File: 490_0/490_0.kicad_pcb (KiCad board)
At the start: 4 copper layers, 208.5 x 137.8 mm, 192 parts, among them J1 PAD, J10 PAD, J11 S3B-XH-A, J12 2000-1-1-20-00-BK, J13 S2B-ZR, J15 S3B-XH-A, J16 DF40HC(3.0)-100DS-0.4V(58), J17 DF40HC(3.0)-100DS-0.4V(58), J18 TS-103-G-A, J19 467650301, J2 PAD, J20 YO0201500000G, J21 TS-102-G-A, J22 2000-1-1-20-00-BK, J23 S3B-XH-A, J3 PAD, J4 PAD, J5 PAD, J6 PAD, J7 629105150521, J8 0526101571, J9 PAD, Q1 AO3400A, Q2 AO3400A, Q3 AO3400A, Q4 AO3400A, Q5 AO3400A, Q6 BSS84, SW1 TL2230EEF140, SW2 TL1105LF160Q, SW3 TL1105LF160Q, SW4 TL1105LF160Q, SW5 TL1105LF160Q, SW6 TL1105LF160Q, SW7 TL1105LF160Q, SW8 TL1105LF160Q, U1 MAX98357A, U10 EMI8142MUTAG, U11 SP3003-02XTG, U12 TPD8S009DSMR, U13 SP3003-02XTG, U14 SP3003-02XTG, U15 SP3003-02XTG, U16 SP3003-02XTG, U17 SP3003-02XTG, U18 TPD8S009DSMR, U19 SP3003-02XTG, U2 TPS2553DBVR, U3 TPS2553DBVR, U4 USB2512B-I/M2, U5 TS3USB221AQRSERQ1, U6 PCA9685, U7 TPS566247DRLR, U8 MP2639AGR-Z, U9 EMI8142MUTAG, Y1 24M20P2/XT324-10/10

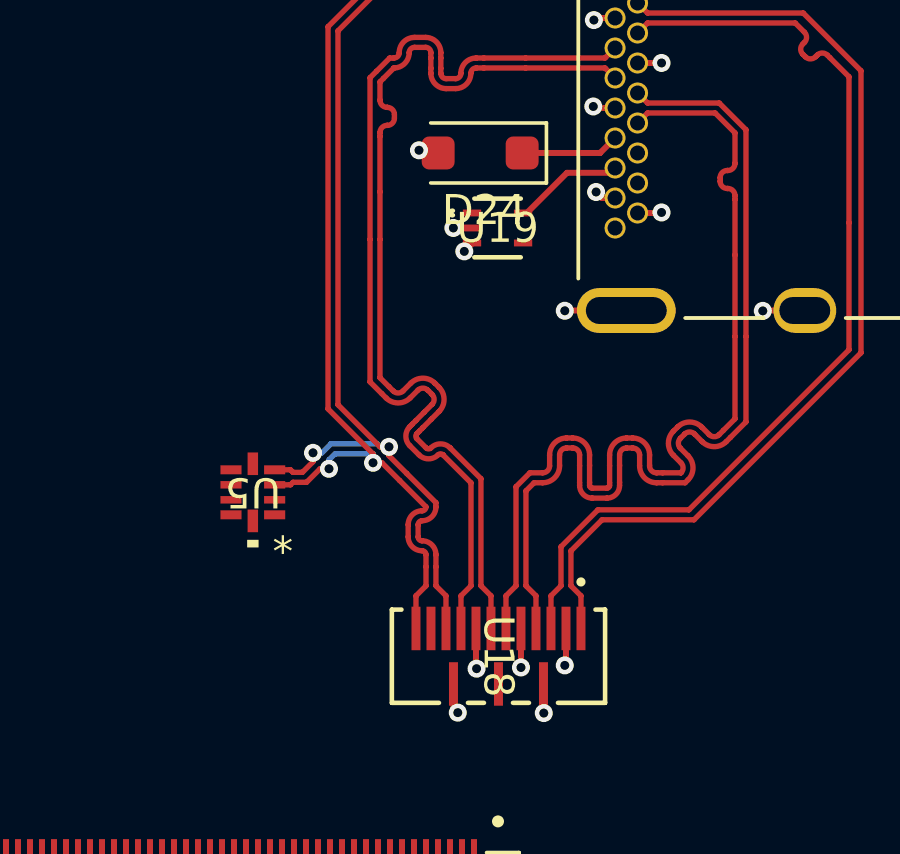
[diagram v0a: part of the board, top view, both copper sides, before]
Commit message: Finished ESD diff pairs routing
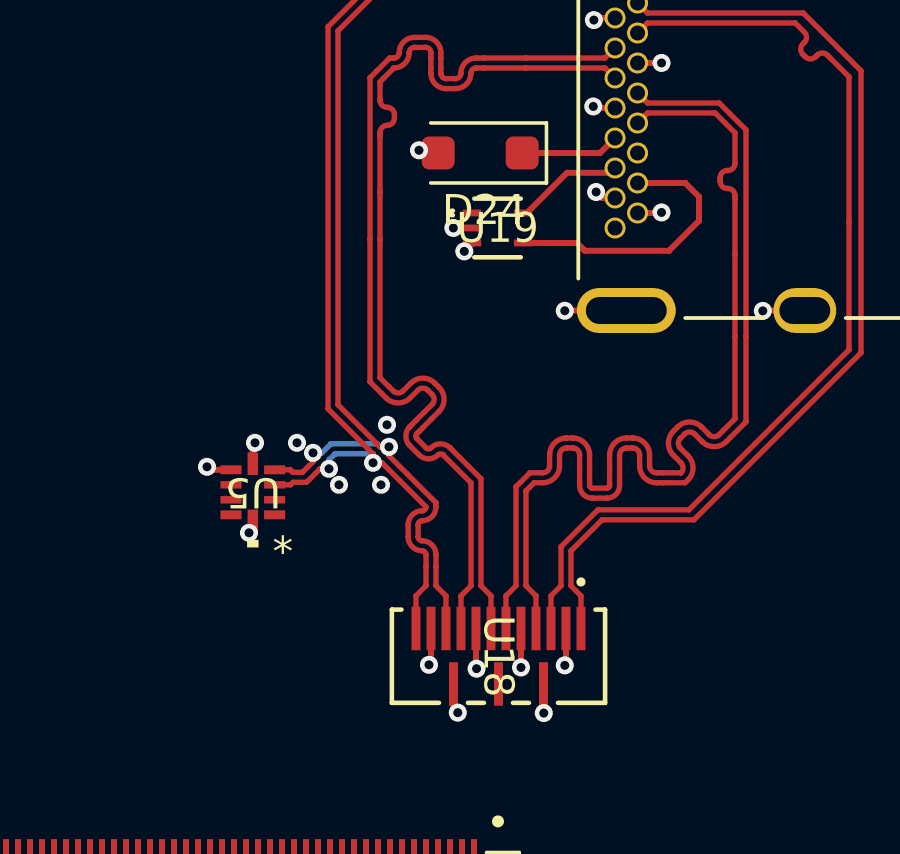
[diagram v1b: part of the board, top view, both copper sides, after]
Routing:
- net /PCB1/PCB1-Board Connector A/SDA1: track 0.00 -> 9.43 mm
- net GND: track 22.3 -> 25.1 mm, vias 17 -> 24
- net +3.3V: track 3.26 -> 3.71 mm, vias 4 -> 5
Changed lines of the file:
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@@
 	)
 	(segment
+		(start 127.865988 127.934012)
+		(end 127.8 128)
+		(width 0.2)
+		(layer "F.Cu")
+		(net 2)
+	)
+	(segment
 		(start 138.786889 101.689655)
 		(end 138.775989 101.678755)
@@
 	)
 	(segment
+		(start 121.9274 121.297556)
+		(end 121.9274 120.6726)
+		(width 0.2)
+		(layer "F.Cu")
+		(net 2)
+	)
+	(segment
 		(start 138.939513 116.189655)
 		(end 138.92689 116.202278)
@@
 	)
 	(segment
+		(start 121.9274 120.6726)
+		(end 122 120.6)
+		(width 0.2)
+		(layer "F.Cu")
+		(net 2)
+	)
+	(segment
 		(start 133.326889 109.439655)
 		(end 133.275989 109.388755)
@@
 	)
 	(segment
+		(start 127.865988 126.788755)
+		(end 127.865988 127.934012)
+		(width 0.2)
+		(layer "F.Cu")
+		(net 2)
+	)
+	(segment
 		(start 133.365089 106.439655)
 		(end 133.295989 106.508755)
@@
 	)
 	(segment
+		(start 120.499999 121.499999)
+		(end 120.4 121.4)
+		(width 0.2)
+		(layer "F.Cu")
+		(net 2)
+	)
+	(segment
+		(start 121.2 121.499999)
+		(end 120.499999 121.499999)
+		(width 0.2)
+		(layer "F.Cu")
+		(net 2)
+	)
+	(segment
 		(start 124.82 87.96)
 		(end 124.82 87.21)
@@
 	)
 	(via
+		(at 126.2 122)
+		(size 0.6)
+		(drill 0.3)
+		(layers "F.Cu" "B.Cu")
+		(net 2)
+	)
+	(via
 		(at 133.295989 106.508755)
 		(size 0.6)
@@
 	)
 	(via
+		(at 127.8 128)
+		(size 0.6)
+		(drill 0.3)
+		(layers "F.Cu" "B.Cu")
+		(net 2)
+	)
+	(via
 		(at 128.611366 113.438757)
 		(size 0.6)
@@
 	)
 	(via
+		(at 124.8 122)
+		(size 0.6)
+		(drill 0.3)
+		(layers "F.Cu" "B.Cu")
+		(net 2)
+	)
+	(via
+		(at 120.4 121.4)
+		(size 0.6)
+		(drill 0.3)
+		(layers "F.Cu" "B.Cu")
+		(net 2)
+	)
+	(via
 		(at 122.07 89.71)
 		(size 0.6)
@@
 		(net 2)
 	)
+	(via
+		(at 122 120.6)
+		(size 0.6)
+		(drill 0.3)
+		(layers "F.Cu" "B.Cu")
+		(net 2)
+	)
+	(via
+		(at 123.4 120.6)
+		(size 0.6)
+		(drill 0.3)
+		(layers "F.Cu" "B.Cu")
+		(net 2)
+	)
+	(via
+		(at 126.4 120)
+		(size 0.6)
+		(drill 0.3)
+		(layers "F.Cu" "B.Cu")
+		(net 2)
+	)
 	(segment
 		(start 131.615989 128.638637)
@@
 	)
 	(segment
+		(start 121.9274 123.4726)
+		(end 121.8 123.6)
+		(width 0.2)
+		(layer "F.Cu")
+		(net 3)
+	)
+	(segment
 		(start 128.615989 129.578755)
 		(end 128.631678 129.594444)
@@
 		(net 3)
 	)
+	(segment
+		(start 121.9274 123.202444)
+		(end 121.9274 123.4726)
+		(width 0.2)
+		(layer "F.Cu")
+		(net 3)
+	)
+	(via
+		(at 121.8 123.6)
+		(size 0.6)
+		(drill 0.3)
+		(layers "F.Cu" "B.Cu")
+		(net 3)
+	)
 	(via
 		(at 128.75989 129.594444)
@@
 	)
 	(segment
+		(start 136.8 113.2)
+		(end 136.8 112.4)
+		(width 0.2)
+		(layer "F.Cu")
+		(net 114)
+	)
+	(segment
+		(start 135.8 114.2)
+		(end 136.8 113.2)
+		(width 0.2)
+		(layer "F.Cu")
+		(net 114)
+	)
+	(segment
+		(start 132.738755 113.938755)
+		(end 133 114.2)
+		(width 0.2)
+		(layer "F.Cu")
+		(net 114)
+	)
+	(segment
+		(start 130.935989 113.938755)
+		(end 132.738755 113.938755)
+		(width 0.2)
+		(layer "F.Cu")
+		(net 114)
+	)
+	(segment
+		(start 133 114.2)
+		(end 135.8 114.2)
+		(width 0.2)
+		(layer "F.Cu")
+		(net 114)
+	)
+	(segment
+		(start 136.8 112.4)
+		(end 136.339655 111.939655)
+		(width 0.2)
+		(layer "F.Cu")
+		(net 114)
+	)
+	(segment
+		(start 136.339655 111.939655)
+		(end 134.751811 111.939655)
+		(width 0.2)
+		(layer "F.Cu")
+		(net 114)
+	)
+	(segment

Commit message: Changed microHDMI to normal HDMI because of the footprint
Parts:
- moved C50 215.2 mm to (173.4, 129.6), turned to 90 degrees
- moved J19 213.2 mm to (176.4, 138.4)
- moved U13 211.2 mm to (171.3, 127.1)
- moved U14 210.0 mm to (167.3, 128.1)
- moved U10 209.5 mm to (170.4, 136.0), turned to 180 degrees
- moved U9 209.3 mm to (177.0, 127.2)
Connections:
- J19 pad 11: Net-(J19-TMDS_DATA_0-) -> /PCB1/PCB1-HDMI/D0-
- J19 pad 12: Net-(J19-TMDS_CLOCK+) -> /PCB1/PCB1-HDMI/CLK+
- J19 pad 14: Net-(J19-TMDS_CLOCK-) -> /PCB1/PCB1-HDMI/CLK-
- J19 pad 3: Net-(J19-TMDS_DATA_2+) -> /PCB1/PCB1-HDMI/D2-
- J19 pad 5: Net-(J19-TMDS_DATA_2-) -> /PCB1/PCB1-HDMI/D2+
- J19 pad 6: Net-(J19-TMDS_DATA_1+) -> /PCB1/PCB1-HDMI/D1-
- J19 pad 8: Net-(J19-TMDS_DATA_1-) -> /PCB1/PCB1-HDMI/D1+
- J19 pad 9: Net-(J19-TMDS_DATA_0+) -> /PCB1/PCB1-HDMI/D0+
- U10 pad 1: Net-(J19-TMDS_DATA_0+) -> unconnected-(U10-IN_1+-Pad1)
- U10 pad 10: /PCB1/PCB1-Board Connector A/HDMI0_TX0_P -> /PCB1/PCB1-Board Connector A/HDMI0_TX1_P
- U10 pad 2: Net-(J19-TMDS_DATA_0-) -> unconnected-(U10-IN_1−-Pad2)
- U10 pad 4: Net-(J19-TMDS_CLOCK+) -> unconnected-(U10-IN_2+-Pad4)
- U10 pad 5: Net-(J19-TMDS_CLOCK-) -> unconnected-(U10-IN_2--Pad5)
- U10 pad 9: /PCB1/PCB1-Board Connector A/HDMI0_TX0_N -> /PCB1/PCB1-Board Connector A/HDMI0_TX1_N
- U9 pad 1: Net-(J19-TMDS_DATA_1+) -> /PCB1/PCB1-HDMI/D0-
- U9 pad 10: /PCB1/PCB1-Board Connector A/HDMI0_TX1_N -> /PCB1/PCB1-Board Connector A/HDMI0_TX0_N
- U9 pad 2: Net-(J19-TMDS_DATA_1-) -> /PCB1/PCB1-HDMI/D0+
- U9 pad 4: Net-(J19-TMDS_DATA_2+) -> /PCB1/PCB1-HDMI/D2+
- U9 pad 5: Net-(J19-TMDS_DATA_2-) -> /PCB1/PCB1-HDMI/D2-
- U9 pad 6: /PCB1/PCB1-Board Connector A/HDMI0_TX2_P -> /PCB1/PCB1-Board Connector A/HDMI0_TX2_N
- U9 pad 7: /PCB1/PCB1-Board Connector A/HDMI0_TX2_N -> /PCB1/PCB1-Board Connector A/HDMI0_TX2_P
- U9 pad 9: /PCB1/PCB1-Board Connector A/HDMI0_TX1_P -> /PCB1/PCB1-Board Connector A/HDMI0_TX0_P
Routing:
- net /PCB1/PCB1-Board Connector A/USB_N: track 0.00 -> 21.1 mm
- net /PCB1/PCB1-Board Connector A/USB_P: track 0.00 -> 20.2 mm
- net +5V: track 7.64 -> 9.71 mm
- net GND: track 25.1 -> 26.1 mm, vias 24 -> 25

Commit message: Routing ESD to 100 pin connector
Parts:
- removed J19: 467650301, *CapStone*:MOLEX_467650301
- added J14: 2000-1-1-20-00-BK, *CapStone*:CNCTECH_2000-1-1-20-00-BK, F.Cu at (114.9, 159.5)
- moved D11 187.2 mm to (-90.8, 152.5)
- moved D12 187.2 mm to (-90.8, 148.5)
- moved D13 187.2 mm to (-91.0, 144.5)
- moved D14 187.2 mm to (-90.8, 140.5)
- moved R28 187.2 mm to (-85.8, 152.5)
- moved R30 187.2 mm to (-85.8, 148.5)
- moved R31 187.2 mm to (-86.0, 144.5)
- moved R33 187.2 mm to (-86.3, 140.5)
- moved U10 68.5 mm to (105.2, 157.2)
- moved C50 68.1 mm to (108.2, 149.3)
- moved U13 62.1 mm to (112.6, 147.2)
- moved U14 60.3 mm to (110.1, 147.1)
- moved U9 59.8 mm to (119.2, 142.5), turned to 180 degrees
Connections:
- U10 pad 1: unconnected-(U10-IN_1+-Pad1) -> /PCB1/PCB1-HDMI/D1-
- U10 pad 10: /PCB1/PCB1-Board Connector A/HDMI0_TX1_P -> /PCB1/PCB1-Board Connector A/HDMI0_TX1_N
- U10 pad 2: unconnected-(U10-IN_1−-Pad2) -> /PCB1/PCB1-HDMI/D1+
- U10 pad 4: unconnected-(U10-IN_2+-Pad4) -> /PCB1/PCB1-HDMI/CLK+
- U10 pad 5: unconnected-(U10-IN_2--Pad5) -> /PCB1/PCB1-HDMI/CLK-
- U10 pad 9: /PCB1/PCB1-Board Connector A/HDMI0_TX1_N -> /PCB1/PCB1-Board Connector A/HDMI0_TX1_P
- U13 pad 4: /PCB1/PCB1-Board Connector A/HDMI0_SCL -> /PCB1/PCB1-Board Connector A/HDMI0_CEC
- U14 pad 5: /PCB1/PCB1-Board Connector A/HDMI0_CEC -> /PCB1/PCB1-Board Connector A/HDMI0_SCL
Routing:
- net /PCB1/PCB1-Board Connector A/HDMI0_TX1_P: track 0.00 -> 42.1 mm, vias 0 -> 2
- net /PCB1/PCB1-Board Connector A/HDMI0_TX1_N: track 0.00 -> 40.5 mm, vias 0 -> 2
- net /PCB1/PCB1-Board Connector A/HDMI0_CLK_P: track 0.00 -> 35.7 mm, vias 0 -> 2
- net /PCB1/PCB1-Board Connector A/HDMI0_CLK_N: track 0.00 -> 34.1 mm, vias 0 -> 2
- net /PCB1/PCB1-Board Connector A/HDMI0_SDA: track 0.00 -> 25.1 mm
- net /PCB1/PCB1-HDMI/D1-: track 0.00 -> 15.3 mm
- net /PCB1/PCB1-HDMI/D2-: track 0.00 -> 15.3 mm
- net /PCB1/PCB1-HDMI/D1+: track 0.00 -> 15.3 mm
- net /PCB1/PCB1-HDMI/D2+: track 0.00 -> 15.2 mm
- net /PCB1/PCB1-HDMI/D0+: track 0.00 -> 15.2 mm
- net /PCB1/PCB1-HDMI/D0-: track 0.00 -> 15.2 mm
- net /PCB1/PCB1-HDMI/CLK+: track 0.00 -> 11.2 mm
- net /PCB1/PCB1-HDMI/CLK-: track 0.00 -> 10.7 mm
- net /PCB1/PCB1-Board Connector A/HDMI0_TX2_N: track 0.00 -> 10.6 mm, vias 0 -> 2
- net /PCB1/PCB1-Board Connector A/HDMI0_TX0_N: track 0.00 -> 10.3 mm
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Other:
- board size 208.5 x 137.8 mm -> 208.5 x 141.2 mm

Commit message: Final push
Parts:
- moved U9 6.88 mm to (124.0, 147.4)
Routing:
- net /PCB1/PCB1-Board Connector A/HDMI0_TX0_N: track 10.3 -> 0.00 mm
- net /PCB1/PCB1-Board Connector A/HDMI0_TX0_P: track 9.77 -> 0.00 mm
- net /PCB1/PCB1-Board Connector A/HDMI0_TX1_P: track 42.1 -> 35.1 mm
- net /PCB1/PCB1-Board Connector A/HDMI0_TX1_N: track 40.5 -> 35.7 mm
- net /PCB1/PCB1-Board Connector A/HDMI0_TX2_P: track 10.1 -> 13.8 mm
- net /PCB1/PCB1-Board Connector A/HDMI0_TX2_N: track 10.6 -> 13.2 mm
- net /PCB1/PCB1-HDMI/D2+: track 15.2 -> 14.6 mm
- net /PCB1/PCB1-HDMI/D0-: track 15.2 -> 14.6 mm

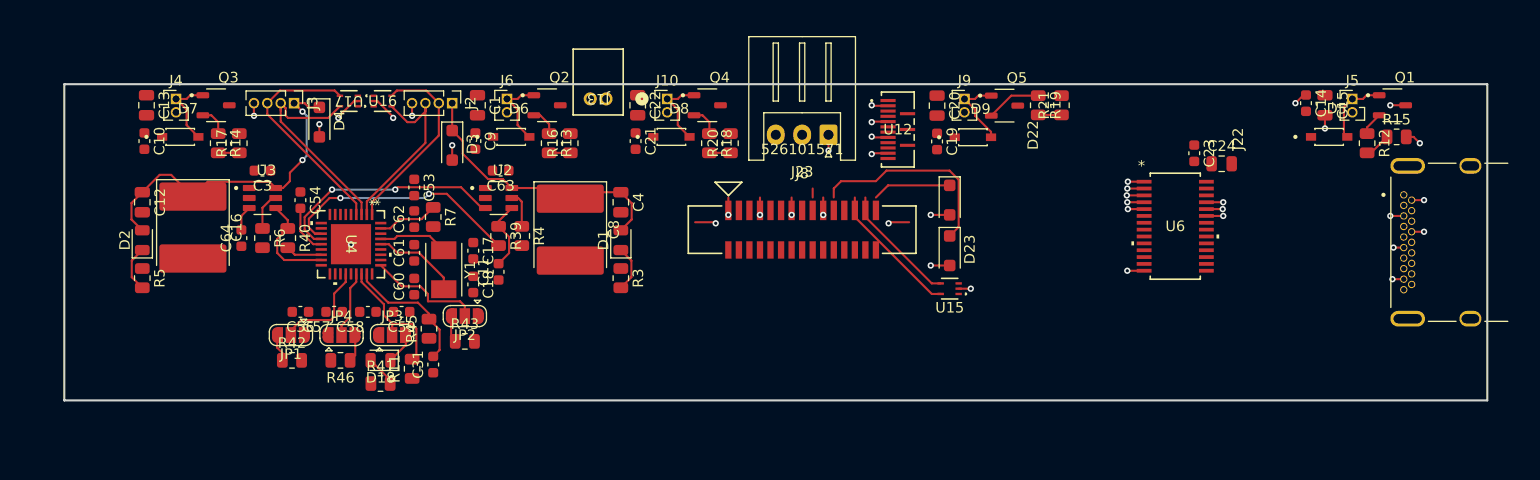
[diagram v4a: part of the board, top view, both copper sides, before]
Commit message: PCB merged, now schematic
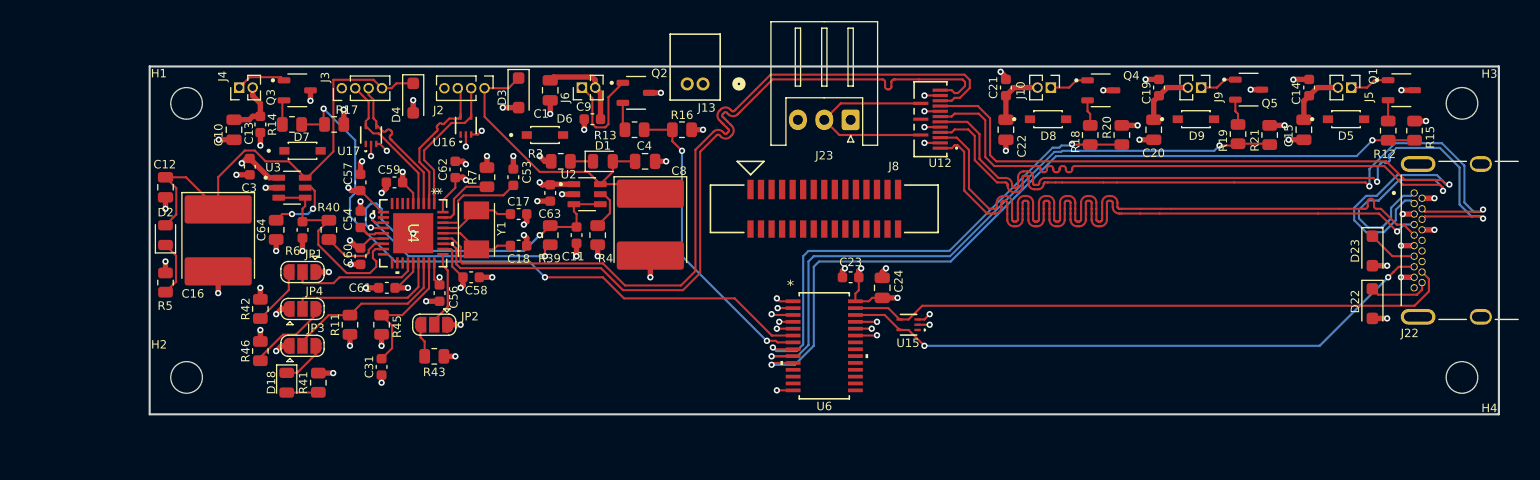
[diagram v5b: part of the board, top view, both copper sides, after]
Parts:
- added H1: MountingHole, MountingHole:MountingHole_3mm, F.Cu at (131.6, 22.0)
- added H2: MountingHole, MountingHole:MountingHole_3mm, F.Cu at (131.6, 48.0)
- added H3: MountingHole, MountingHole:MountingHole_3mm, F.Cu at (252.6, 22.0)
- added H4: MountingHole, MountingHole:MountingHole_3mm, F.Cu at (252.6, 48.0)
- moved D22 41.3 mm to (244.1, 41.0)
- moved D23 40.1 mm to (244.1, 36.0)
- moved Q4 37.4 mm to (218.3, 20.8)
- moved R20 37.1 mm to (220.3, 25.0)
- moved J10 36.4 mm to (213.6, 20.5), turned to -90 degrees
- moved R18 36.1 mm to (217.3, 25.0)
- moved D8 35.8 mm to (213.3, 23.5)
- moved C21 35.5 mm to (209.3, 20.5)
- moved U6 35.2 mm to (192.1, 45.0)
- moved C22 35.0 mm to (209.3, 24.5)
- moved C23 34.7 mm to (194.6, 38.5), turned to 0 degrees
- moved C24 34.3 mm to (197.6, 39.5), turned to 90 degrees
- moved Q5 23.2 mm to (232.4, 20.7)
- moved J9 22.5 mm to (227.9, 20.5), turned to -90 degrees
- moved C19 21.7 mm to (223.9, 20.5)
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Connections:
- net Net-(J22-D0+) renamed /PCB2/D0+
- net Net-(J22-D0-) renamed /PCB2/D0-
- net Net-(J22-D1+) renamed /PCB2/D1+
- net Net-(J22-D1-) renamed /PCB2/D1-
- J22 pad 1: /PCB2/PCB2-USB 2.0 Bridge/USB_P -> /PCB2/CK+
- J22 pad 10: Net-(J22-CK+) -> /PCB2/CK+
- J22 pad 12: Net-(J22-CK-) -> /PCB2/CK-
- J22 pad 3: /PCB2/PCB2-USB 2.0 Bridge/USB_N -> /PCB2/CK-
- J3 pad 1: VBUS2 -> GND_GLASSES
- J3 pad 2: /PCB2/PCB2-USB 2.0 Bridge/D2- -> /PCB2/PCB2-USB 2.0 Bridge/D2+
- J3 pad 3: /PCB2/PCB2-USB 2.0 Bridge/D2+ -> /PCB2/PCB2-USB 2.0 Bridge/D2-
- J3 pad 4: GND_GLASSES -> VBUS2
- U12 pad 10: /PCB2/PCB2-USB 2.0 Bridge/USB_P -> /PCB2/CK+
- U12 pad 12: /PCB2/PCB2-USB 2.0 Bridge/USB_N -> /PCB2/CK-
- U12 pad 7: Net-(J22-CK+) -> /PCB2/CK+
- U12 pad 9: Net-(J22-CK-) -> /PCB2/CK-
- U16 pad 4: /PCB2/PCB2-USB 2.0 Bridge/D1+ -> /PCB2/PCB2-USB 2.0 Bridge/D1-
- U16 pad 5: /PCB2/PCB2-USB 2.0 Bridge/D1- -> /PCB2/PCB2-USB 2.0 Bridge/D1+
- U17 pad 4: /PCB2/PCB2-USB 2.0 Bridge/D2+ -> /PCB2/PCB2-USB 2.0 Bridge/D2-
- U17 pad 5: /PCB2/PCB2-USB 2.0 Bridge/D2- -> /PCB2/PCB2-USB 2.0 Bridge/D2+
- U4 pad 30: /PCB2/PCB2-USB 2.0 Bridge/USB_N -> /PCB2/CK-
- U4 pad 31: /PCB2/PCB2-USB 2.0 Bridge/USB_P -> /PCB2/CK+
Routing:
- net /PCB2/CK-: track 0.00 -> 148.3 mm, vias 0 -> 1
- net /PCB2/CK+: track 0.00 -> 148.2 mm, vias 0 -> 1
- net /PCB2/D0-: track 0.00 -> 74.5 mm
- net /PCB2/PCB2-PWM and Motors/PWM4: track 2.51 -> 76.3 mm, vias 0 -> 2
- net /PCB2/D0+: track 0.00 -> 73.0 mm, vias 0 -> 1
- net /PCB2/D1+: track 0.00 -> 71.7 mm, vias 0 -> 2
- net /PCB2/D1-: track 0.00 -> 71.7 mm, vias 0 -> 2
- net +3.3V_GLASSES: track 0.00 -> 71.4 mm, vias 0 -> 17
- net /PCB2/PCB2-PWM and Motors/PWM3: track 2.20 -> 62.4 mm, vias 0 -> 2
- net /PCB2/PCB2-PWM and Motors/PWM0: track 2.00 -> 62.1 mm, vias 0 -> 2
- net /PCB2/PCB2-PWM and Motors/PWM2: track 2.00 -> 49.0 mm, vias 0 -> 2
- net /PCB2/PCB2-PWM and Motors/I2C_SDA: track 11.6 -> 58.1 mm
- net /PCB2/PCB2-PWM and Motors/I2C_SCL: track 13.0 -> 57.4 mm, vias 0 -> 2
- net GND_GLASSES: track 58.8 -> 101.7 mm, vias 39 -> 80
- net +5V_GLASSES: track 0.00 -> 33.2 mm, vias 0 -> 2
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- added copper zone on In2.Cu, net +3.3V_GLASSES
- added copper zone on In2.Cu, net +5V_GLASSES
- added copper zone on In1.Cu, net GND_GLASSES
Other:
- board size 208.5 x 141.2 mm -> 209.6 x 142.9 mm
